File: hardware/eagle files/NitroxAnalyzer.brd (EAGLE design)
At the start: 100 x 80 mm, 16 parts

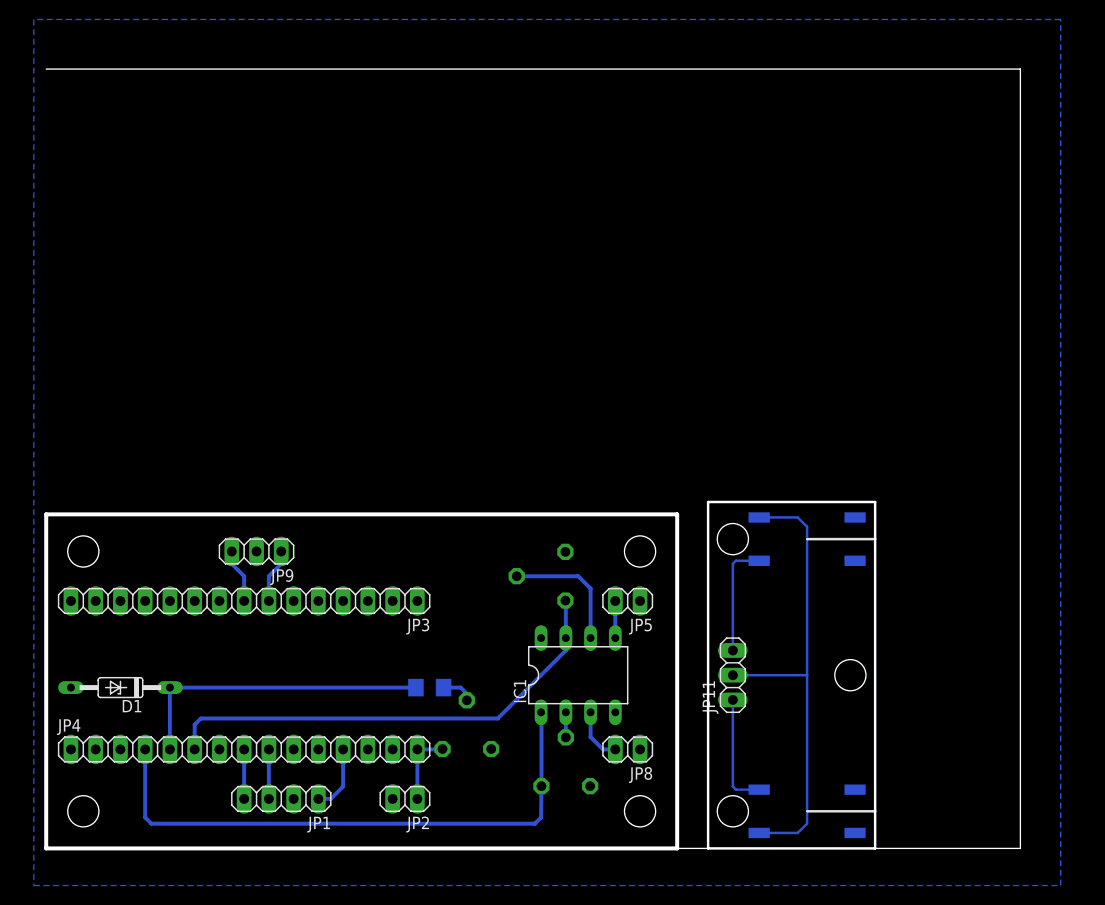
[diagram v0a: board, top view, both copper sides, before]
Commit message: Updated a bit the buttons hardware board to better match the 3d box
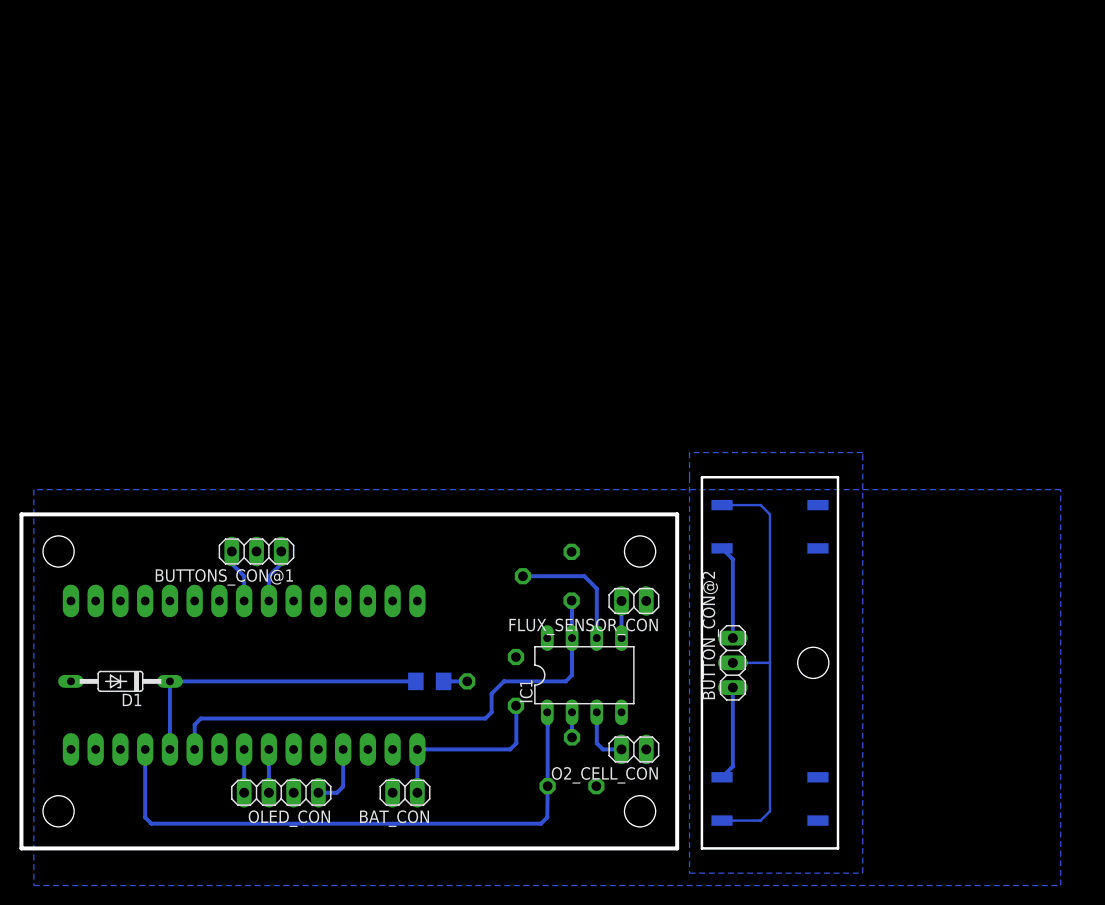
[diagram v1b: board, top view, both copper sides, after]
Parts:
- removed JP1: (no value), pinhead:1X04
- removed JP11: (no value), pinhead:1X03
- removed JP2, JP5, JP8: (no value), pinhead:1X02
- removed JP3, JP4: (no value), pinhead:1X15
- added BAT_CON, FLUX_SENSOR_CON, O2_CELL_CON: (no value), pinhead:1X02
- added BUTTON_CON@2: (no value), pinhead:1X03
- added OLED_CON: (no value), pinhead:1X04
- added U$4: DIL30, ic-package:DIL30
- moved U$1 5.12 mm to (45.7, 17.1), turned to 90 degrees
- moved CALIBRATE 4.02 mm to (74.3, 33.0)
- moved START 4.02 mm to (74.3, 5.08)
- moved U$3 0.64 mm to (51.4, 27.9)
- moved D1 0.63 mm to (7.62, 17.1)
- moved IC1 0.63 mm to (55.2, 17.8)
- moved R1 0.63 mm to (39.4, 17.1)
- moved U$2 0.63 mm to (54.0, 8.89)
- renumbered JP9 to BUTTONS_CON@1
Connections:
- new net N$10: U$4.P$5
- new net N$11: U$4.P$6
- new net N$12: U$4.P$9
- new net N$13: U$4.P$10
- new net N$14: U$4.P$11
- new net N$15: U$4.P$12
- new net N$16: U$4.P$13
- new net N$17: U$4.P$14
- new net N$18: U$4.P$15
- new net N$19: U$4.P$16
- new net N$2: U$4.P$1
- new net N$20: U$4.P$17
- new net N$21: U$4.P$18
- new net N$22: U$4.P$22
- new net N$23: U$4.P$25
- new net N$24: U$4.P$26
- new net N$25: U$4.P$28
- new net N$7: U$4.P$2
- new net N$9: U$4.P$3
- net +9V: now also BAT_CON.1, U$4.P$30; no longer JP2.1, JP4.15
- net BATTERY_ANALOG: now also U$4.P$20; no longer JP4.5
- net CALIBRATE: now also U$4.P$8; no longer JP3.8
- net FLUX_ANALOG: now also U$4.P$21; no longer JP4.6
- net FLUX_SIGNAL: now also FLUX_SENSOR_CON.2; no longer JP5.2
- net GND: now also BAT_CON.2, FLUX_SENSOR_CON.1, O2_CELL_CON.1, OLED_CON.2, U$4.P$29, U$4.P$4; no longer JP1.2, JP2.2, JP3.4, JP4.14, JP5.1, JP8.1
- net N$4: now also BUTTON_CON@2.3; no longer JP11.3
- net N$6: now also BUTTON_CON@2.1; no longer JP11.1
- net N$8: now also BUTTON_CON@2.2; no longer JP11.2
- net O2_CELL_ANALOG: now also U$4.P$19; no longer JP4.4
- net O2_SIGNAL: now also O2_CELL_CON.2; no longer JP8.2
- net SCL: now also OLED_CON.3, U$4.P$24; no longer JP1.3, JP4.9
- net SDA: now also OLED_CON.4, U$4.P$23; no longer JP1.4, JP4.8
- net START: now also U$4.P$7; no longer JP3.7
- net VCC: now also OLED_CON.1, U$4.P$27; no longer JP1.1, JP4.12
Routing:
- net +9V: track 7.68 -> 18.7 mm
- net N$8: track 48.7 -> 44.9 mm
- net FLUX_ANALOG: track 48.9 -> 52.3 mm
- net N$4: track 11.7 -> 10.3 mm
- net N$6: track 11.7 -> 10.3 mm
- net N$1: track 3.34 -> 2.43 mm
- net BATTERY_ANALOG: track 31.6 -> 32.2 mm
- net SDA: track 5.08 -> 4.45 mm
- net SCL: track 5.08 -> 4.45 mm
- net O2_CELL_ANALOG: track 59.0 -> 59.6 mm
- added copper zone on layer 16, net N$8
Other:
- board size 100 x 80 mm -> 83.8 x 38.1 mm
- board text added: "START"

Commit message: Updated some 3d cad models and other stuff
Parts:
- removed BAT_CON, FLUX_SENSOR_CON, O2_CELL_CON: (no value), pinhead:1X02
- removed BUTTONS_CON@1, BUTTON_CON@2: (no value), pinhead:1X03
- removed OLED_CON: (no value), pinhead:1X04
- added JP1: OLED_CON, pinhead:1X04
- added JP2: BAT_CON, pinhead:1X02
- added JP3: BUTTONS_CON@1, pinhead:1X03
- added JP4: BUTTON_CON@2, pinhead:1X03
- added JP5: O2_CELL_CON, pinhead:1X02
- added JP6: FLUX_SENSOR_CON, pinhead:1X02
- moved D1 2.54 mm to (10.2, 17.1)
- moved IC1 2.54 mm to (57.8, 17.8)
- moved R1 2.54 mm to (41.9, 17.1)
- moved U$1 2.54 mm to (48.3, 17.1)
- moved U$2 2.54 mm to (56.5, 8.89)
- moved U$3 2.54 mm to (54.0, 27.9)
- moved U$4 2.54 mm to (22.9, 17.8)
- moved CALIBRATE 2.54 mm to (76.8, 33.0)
- moved START 2.54 mm to (76.8, 5.08)
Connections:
- net +9V: now also JP2.1; no longer BAT_CON.1
- net CALIBRATE: now also JP3.3; no longer BUTTONS_CON@1.3
- net FLUX_SIGNAL: now also JP6.2; no longer FLUX_SENSOR_CON.2
- net GND: now also JP1.2, JP2.2, JP3.2, JP5.1, JP6.1; no longer BAT_CON.2, BUTTONS_CON@1.2, FLUX_SENSOR_CON.1, O2_CELL_CON.1, OLED_CON.2
- net N$4: now also JP4.3; no longer BUTTON_CON@2.3
- net N$6: now also JP4.1; no longer BUTTON_CON@2.1
- net N$8: now also JP4.2; no longer BUTTON_CON@2.2
- net O2_SIGNAL: now also JP5.2; no longer O2_CELL_CON.2
- net SCL: now also JP1.3; no longer OLED_CON.3
- net SDA: now also JP1.4; no longer OLED_CON.4
- net START: now also JP3.1; no longer BUTTONS_CON@1.1
- net VCC: now also JP1.1; no longer OLED_CON.1
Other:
- outline, holes or cut-outs redrawn

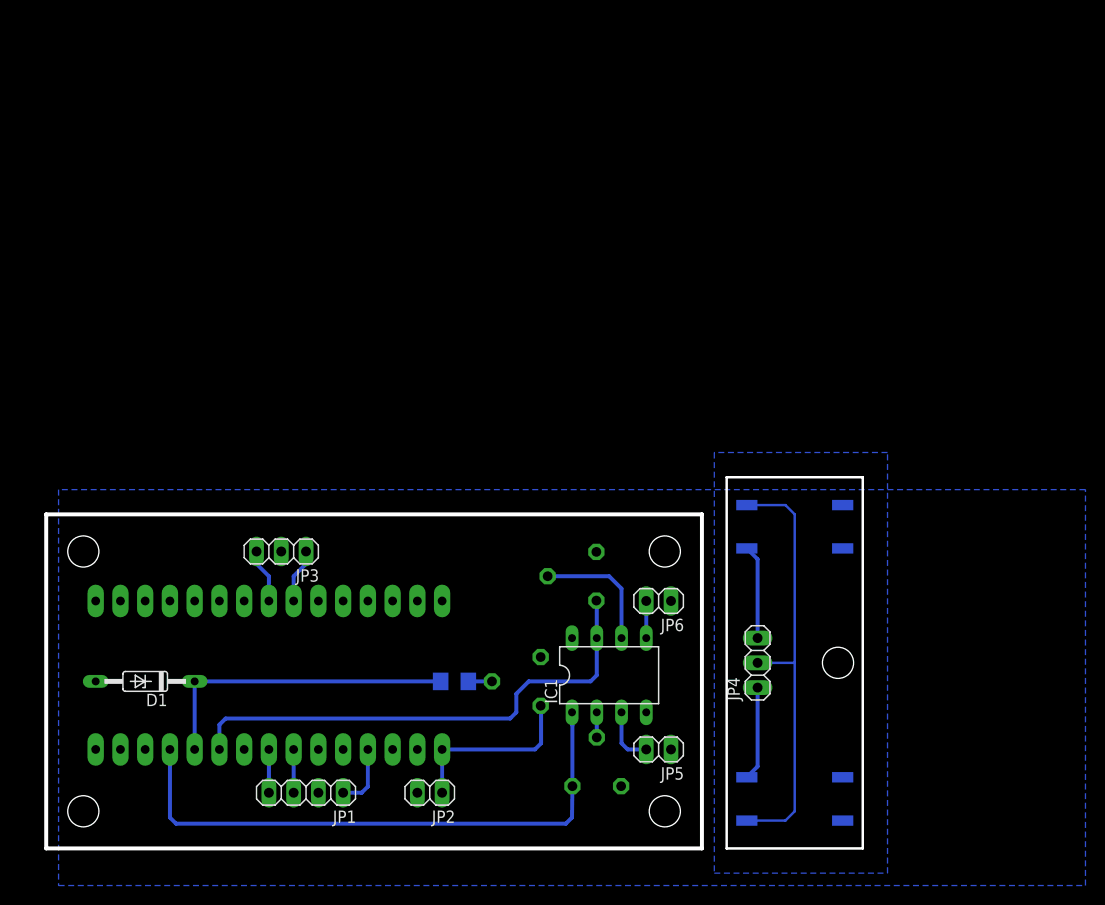
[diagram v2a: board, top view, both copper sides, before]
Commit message: last commit on this solution.
I got some drawbacks that force to change the approach.

1- No more screen and buttons but an Android interface
2- Bluetooth Connection will be used
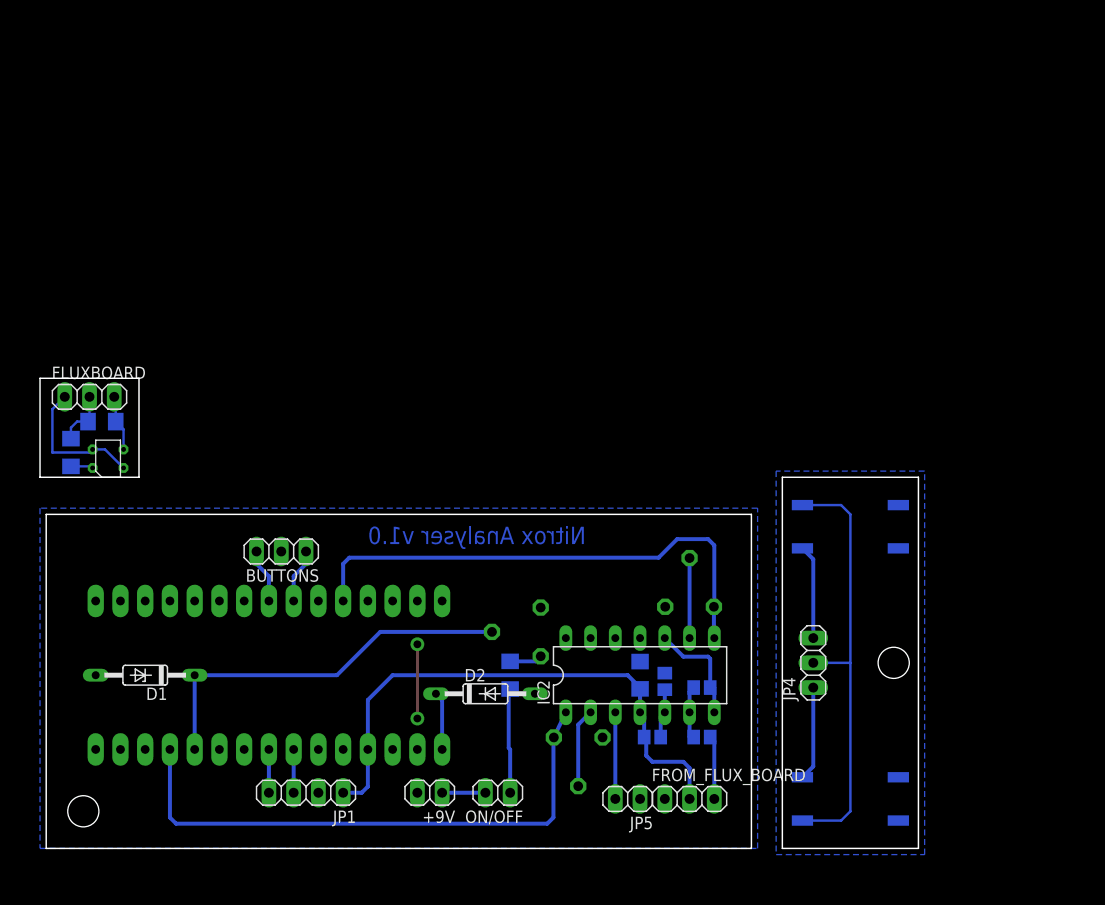
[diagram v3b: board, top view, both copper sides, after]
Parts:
- removed IC1: (no value), linear:DIL08
- removed JP6: FLUX_SENSOR_CON, pinhead:1X02
- added C2: 100n, rcl:C1206
- added D2: BA221, diode:DO35-10
- added FLUXBOARD, FROM_FLUX_BOARD: (no value), pinhead:1X03
- added IC2: LM2902N, linear:DIL14
- added ON/OFF: BAT_CON, pinhead:1X02
- added R100: 220, rcl:R1206
- added R2: 6K, rcl:R1206
- added R3: 10K, rcl:R1206
- added R4, R5, R6: 91K, rcl:R0805
- added U$5: 100K, piher:PT6KV
- BUTTONS: value BUTTONS_CON@1 -> (none)
- R1: value 10k -> 91K; device rcl:R1206 -> rcl:R0805
- U$1: value PT6KV-10k -> 10K
- U$2: value PT6KV-10k -> 100K
- U$3: value PT6KV-10k -> (none); device piher:PT6KV -> ITR8307:4PIN
- moved U$3 49.1 mm to (6.35, 40.0), turned to 0 degrees
- moved R1 21.1 mm to (62.2, 11.4)
- moved JP5 5.99 mm to (59.7, 5.08)
- moved CALIBRATE 5.72 mm to (82.5, 33.0)
- moved START 5.72 mm to (82.5, 5.08)
- moved JP4 5.71 mm to (78.7, 19.1)
- moved U$1 5.08 mm to (48.3, 22.2)
- moved U$2 1.91 mm to (54.6, 8.89), turned to 180 degrees
- moved D1 0.64 mm to (10.2, 17.8)
- renumbered JP2 to +9V, JP3 to BUTTONS
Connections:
- removed net FLUX_SIGNAL: IC1.5, JP6.2
- removed net O2_SIGNAL: IC1.3, JP5.2
- removed net V+: IC1.8
- removed net V-: IC1.4
- new net FLUX_DIGITAL: IC2.8, U$4.P$5, U$5.B
- new net GND_: FLUXBOARD.1, U$3.C, U$3.EMI
- new net N$26: R2.2, U$1.A
- new net N$28: IC2.10, IC2.7, R6.2
- new net N$29: IC2.6, R5.2, R6.1
- new net N$30: FROM_FLUX_BOARD.3, R5.1
- new net N$31: IC2.5, R1.1, R4.2
- new net N$32: IC2.9, U$5.C
- new net N$33: IC2.3, JP5.2
- new net SIG: FLUXBOARD.3, R3.2, U$3.COL
- new net VCC_: FLUXBOARD.2, R100.1, R3.1
- net +9V: now also D2.A, ON/OFF.1, R2.1; no longer +9V.1, U$1.A, U$4.P$30
- net BATTERY_ANALOG: now also U$1.C; no longer R1.2
- net FLUX_ANALOG: no longer IC1.7, U$3.A
- net GND: now also C2.2, FROM_FLUX_BOARD.1, IC2.11, R4.1, U$2.A, U$5.A; no longer JP6.1, U$2.B, U$3.B
- net N$1: now also R100.2, U$3.A; no longer R1.1, U$1.C
- net N$10: now also D2.C, U$4.P$30; no longer U$4.P$5
- net N$3: now also IC2.2; no longer IC1.2
- net N$5: now also +9V.1, ON/OFF.2; no longer IC1.6, U$3.C
- net O2_CELL_ANALOG: now also IC2.1, U$2.B; no longer IC1.1, U$2.A
- net VCC: now also C2.1, FROM_FLUX_BOARD.2, IC2.4, R1.2
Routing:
- net FLUX_DIGITAL: track 0.00 -> 52.8 mm
- net VCC: track 6.61 -> 59.2 mm
- net FLUX_ANALOG: track 52.3 -> 0.00 mm
- net GND_: track 0.00 -> 14.5 mm
- net N$28: track 0.00 -> 11.5 mm
- net N$33: track 0.00 -> 8.89 mm
- net N$5: track 13.2 -> 4.45 mm
- net N$32: track 0.00 -> 8.21 mm
- net BATTERY_ANALOG: track 32.2 -> 40.0 mm
- net GND: track 0.00 -> 7.62 mm, vias 0 -> 2
- net N$30: track 0.00 -> 6.52 mm
- net O2_SIGNAL: track 5.98 -> 0.00 mm
- net N$10: track 0.00 -> 5.98 mm
- net SIG: track 0.00 -> 5.79 mm
- net VCC_: track 0.00 -> 5.74 mm
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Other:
- board size 83.8 x 38.1 mm -> 90.2 x 48.3 mm
- board text added: "Nitrox Analyser v1.0"
